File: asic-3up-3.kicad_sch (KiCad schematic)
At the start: 98 parts, among them J10 Conn_01x01, J11 Conn_01x01, U4 SN74AVC4T774, U5 25MHz, U66 MCP1824T-1202E/OT, U67 MCP1824T-1202E/OT, U68 MCP1824T-1202E/OT, U69 MCP1824T-0802E, U70 MCP1824T-0802E, U71 MCP1824T-0802E, U72 BM1362AC_MODE1, U73 BM1362AC_MODE0, U74 BM1362AC_MODE1

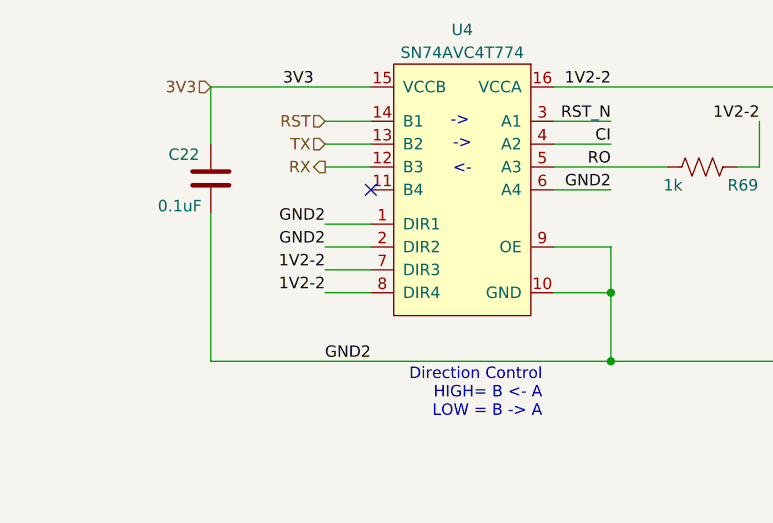
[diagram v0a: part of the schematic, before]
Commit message: change net names for #59. Fix missing symbols
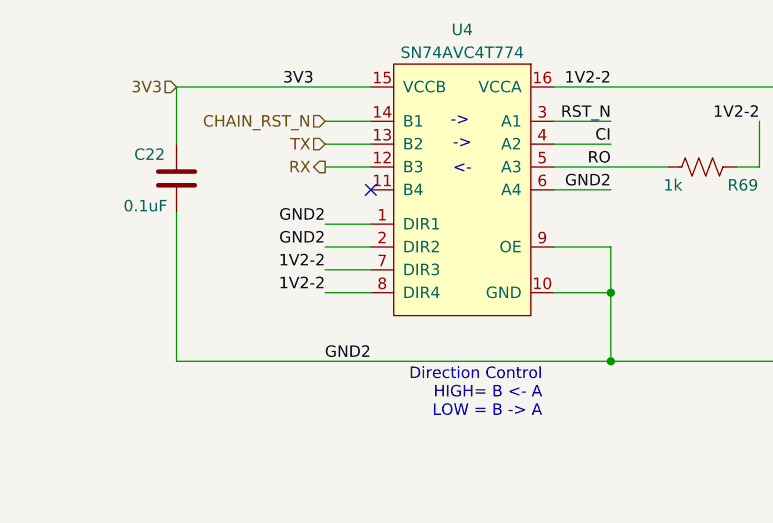
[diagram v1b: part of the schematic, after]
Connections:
- net RST renamed CHAIN_RST_N
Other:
- moved on the sheet: C22
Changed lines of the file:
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@@
 	(wire
 		(pts
-			(xy 71.12 34.29) (xy 53.34 34.29)
+			(xy 71.12 34.29) (xy 49.53 34.29)
 		)
 		(stroke
@@
 	(wire
 		(pts
-			(xy 97.79 64.77) (xy 53.34 64.77)
+			(xy 97.79 64.77) (xy 49.53 64.77)
 		)
 		(stroke
@@
 	(wire
 		(pts
-			(xy 53.34 48.26) (xy 53.34 64.77)
+			(xy 49.53 48.26) (xy 49.53 64.77)
 		)
 		(stroke
@@
 	(wire
 		(pts
-			(xy 53.34 34.29) (xy 53.34 40.64)
+			(xy 49.53 34.29) (xy 49.53 40.64)
 		)
 		(stroke
@@
 		)
 	)
-	(hierarchical_label "RST"
+	(hierarchical_label "CHAIN_RST_N"
 		(shape input)
 		(at 66.04 38.1 180)
@@
 	(hierarchical_label "3V3"
 		(shape input)
-		(at 53.34 34.29 180)
+		(at 49.53 34.29 180)
 		(effects
 			(font
@@
 			)
 		)
-		(property "Description" ""
+		(property "Description" "Unpolarized capacitor"
 			(at 152.4 170.18 0)
 			(hide yes)
@@
 			)
 		)
-		(property "Description" ""
+		(property "Description" "Unpolarized capacitor"
 			(at 91.44 170.18 0)
 			(hide yes)
@@
 			)
 		)
-		(property "Description" ""
+		(property "Description" "Unpolarized capacitor"
 			(at 363.22 227.33 0)
 			(hide yes)
@@
 			)
 		)
-		(property "Description" ""
+		(property "Description" "Unpolarized capacitor"
 			(at 240.03 134.62 0)
 			(hide yes)
@@
 			)
 		)
-		(property "Description" ""
+		(property "Description" "Unpolarized capacitor"
 			(at 232.41 246.38 0)
 			(hide yes)
@@
 			)
 		)
-		(property "Description" ""
+		(property "Description" "Unpolarized capacitor"
 			(at 57.15 111.76 0)
 			(hide yes)
@@
 			)
 		)
-		(property "Description" ""
+		(property "Description" "test point"
 			(at 100.33 163.83 0)
 			(hide yes)
@@
 			)
 		)
-		(property "Description" ""
+		(property "Description" "Unpolarized capacitor"
 			(at 373.38 111.76 0)
 			(hide yes)
@@
 			)
 		)
-		(property "Description" ""
+		(property "Description" "Unpolarized capacitor"
 			(at 118.11 170.18 0)
 			(hide yes)
@@
 			)
 		)
-		(property "Description" ""
+		(property "Description" "Unpolarized capacitor"
 			(at 121.92 44.45 0)
 			(hide yes)
@@
 			)
 		)
-		(property "Description" ""
+		(property "Description" "Unpolarized capacitor"
 			(at 232.41 134.62 0)
 			(hide yes)
@@
 			)
 		)
-		(property "Description" ""
+		(property "Description" "Unpolarized capacitor"
 			(at 363.22 167.64 0)
 			(hide yes)
@@
 			)
 		)
-		(property "Description" "powertab"
+		(property "Description" "Generic connector, single row, 01x01, script generated (kicad-library-utils/schlib/autogen/connector/)"
 			(at 265.43 194.31 0)
 			(hide yes)
@@
 			)
 		)
-		(property "Description" ""
+		(property "Description" "Unpolarized capacitor"
 			(at 91.44 227.33 0)
 			(hide yes)
@@
 			)
 		)
-		(property "Description" ""
+		(property "Description" "Unpolarized capacitor"
 			(at 118.11 111.76 0)
 			(hide yes)
@@
 			)
 		)
-		(property "Description" ""
+		(property "Description" "test point"
 			(at 346.71 105.41 0)
 			(hide yes)
@@
 			)
 		)
-		(property "Description" ""
+		(property "Description" "Unpolarized capacitor"
 			(at 161.29 53.34 0)
 			(hide yes)
@@
 			)
 		)
-		(property "Description" ""
+		(property "Description" "test point"
 			(at 100.33 105.41 0)
 			(hide yes)
@@
 			)
 		)
-		(property "Description" ""
+		(property "Description" "test point"
 			(at 100.33 220.98 0)
 			(hide yes)
@@
 			)
 		)
-		(property "Description" ""
+		(property "Description" "Unpolarized capacitor"
 			(at 373.38 167.64 0)
 			(hide yes)
@@
 			)
 		)
-		(property "Description" ""
+		(property "Description" "test point"
 			(at 172.72 251.46 0)
 			(hide yes)
@@
 			)
 		)
-		(property "Description" ""
+		(property "Description" "Unpolarized capacitor"
 			(at 57.15 227.33 0)
 			(hide yes)
@@
 			)
 		)
-		(property "Description" ""
+		(property "Description" "test point"
 			(at 172.72 246.38 0)
 			(hide yes)
@@
 			)
 		)
-		(property "Description" ""
+		(property "Description" "Unpolarized capacitor"
 			(at 363.22 111.76 0)
 			(hide yes)
@@
 			)
 		)
-		(property "Description" "powertab"
+		(property "Description" "Generic connector, single row, 01x01, script generated (kicad-library-utils/schlib/autogen/connector/)"
 			(at 265.43 137.16 0)
 			(hide yes)
@@
 	)
 	(symbol
-		(lib_name "MCP1824_1")
 		(lib_id "bitaxe:MCP1824")
 		(at 137.16 106.68 0)
@@
 			)
 		)
-		(property "Description" ""
+		(property "Description" "test point"
 			(at 172.72 248.92 0)
 			(hide yes)
@@
 			)
 		)
-		(property "Description" ""
+		(property "Description" "Unpolarized capacitor"
 			(at 152.4 111.76 0)
 			(hide yes)
@@
 			)
 		)
-		(property "Description" ""
+		(property "Description" "test point"
 			(at 160.02 163.83 0)
 			(hide yes)
@@
 			)
 		)
-		(property "Description" ""
+		(property "Description" "Unpolarized capacitor"
 			(at 240.03 246.38 0)
 			(hide yes)
@@
 	)
 	(symbol
-		(lib_name "MCP1824_1")
 		(lib_id "bitaxe:MCP1824")
 		(at 137.16 165.1 0)
@@
 			)
 		)
-		(property "Description" ""
+		(property "Description" "test point"
 			(at 172.72 243.84 0)
 			(hide yes)
@@
 	)
 	(symbol
-		(lib_name "MCP1824_1")
 		(lib_id "bitaxe:MCP1824")
 		(at 137.16 222.25 0)
@@
 			)
 		)
-		(property "Description" ""
+		(property "Description" "Unpolarized capacitor"
 			(at 118.11 227.33 0)
 			(hide yes)
@@
 			)
 		)
-		(property "Description" ""
+		(property "Description" "test point"
 			(at 160.02 220.98 0)
 			(hide yes)
@@
 			)
 		)
-		(property "Description" ""
+		(property "Description" "Unpolarized capacitor"
 			(at 91.44 111.76 0)
 			(hide yes)
@@
 			)
 		)
-		(property "Description" ""
+		(property "Description" "Unpolarized capacitor"
 			(at 373.38 227.33 0)
 			(hide yes)
@@
 	(symbol
 		(lib_id "Device:C")
-		(at 53.34 44.45 0)
+		(at 49.53 44.45 0)
 		(mirror y)
 		(unit 1)
@@
 		(dnp no)
 		(property "Reference" "C22"
-			(at 52.07 42.545 0)
+			(at 48.26 42.545 0)
 			(show_name no)
 			(do_not_autoplace no)
@@
 		)
 		(property "Value" "0.1uF"
-			(at 52.324 48.26 0)
+			(at 48.514 48.26 0)
 			(show_name no)
 			(do_not_autoplace no)
@@
 		)
 		(property "Footprint" "Capacitor_SMD:C_0402_1005Metric"
-			(at 53.34 44.45 0)
+			(at 49.53 44.45 0)
 			(hide yes)
 			(show_name no)
@@
 		)
 		(property "Datasheet" ""
-			(at 53.34 44.45 0)
+			(at 49.53 44.45 0)
 			(hide yes)
 			(show_name no)
@@
 			)
 		)
-		(property "Description" ""
-			(at 53.34 44.45 0)
+		(property "Description" "Unpolarized capacitor"
+			(at 49.53 44.45 0)
 			(hide yes)
 			(show_name no)
@@
 		)
 		(property "DK" "478-KGM05AR71C104KHCT-ND"
-			(at 53.34 44.45 0)
+			(at 49.53 44.45 0)
 			(hide yes)
 			(show_name no)
@@
 		)
 		(property "PARTNO" "KGM05AR71C104KH"
-			(at 53.34 44.45 0)
+			(at 49.53 44.45 0)
 			(hide yes)
 			(show_name no)
@@
 		)
 		(property "LCSC" "C307331"
-			(at 53.34 44.45 0)
+			(at 49.53 44.45 0)
 			(hide yes)
 			(show_name no)
@@
 		)
 		(property "Field6" ""
-			(at 53.34 44.45 0)
+			(at 49.53 44.45 0)
 			(hide yes)
 			(show_name no)
@@
 			)
 		)
-		(property "Description" ""
+		(property "Description" "Unpolarized capacitor"
 			(at 57.15 170.18 0)
 			(hide yes)
@@
 			)
 		)
-		(property "Description" ""
+		(property "Description" "Unpolarized capacitor"
 			(at 240.03 190.5 0)
 			(hide yes)
@@
 			)
 		)
-		(property "Description" ""
+		(property "Description" "test point"
 			(at 160.02 105.41 0)
 			(hide yes)
@@
 			)
 		)
-		(property "Description" ""
+		(property "Description" "Unpolarized capacitor"
 			(at 232.41 190.5 0)
 			(hide yes)
@@
 			)
 		)
-		(property "Description" ""
+		(property "Description" "Unpolarized capacitor"
 			(at 152.4 227.33 0)
 			(hide yes)
